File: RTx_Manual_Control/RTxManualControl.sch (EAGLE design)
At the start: 36 parts

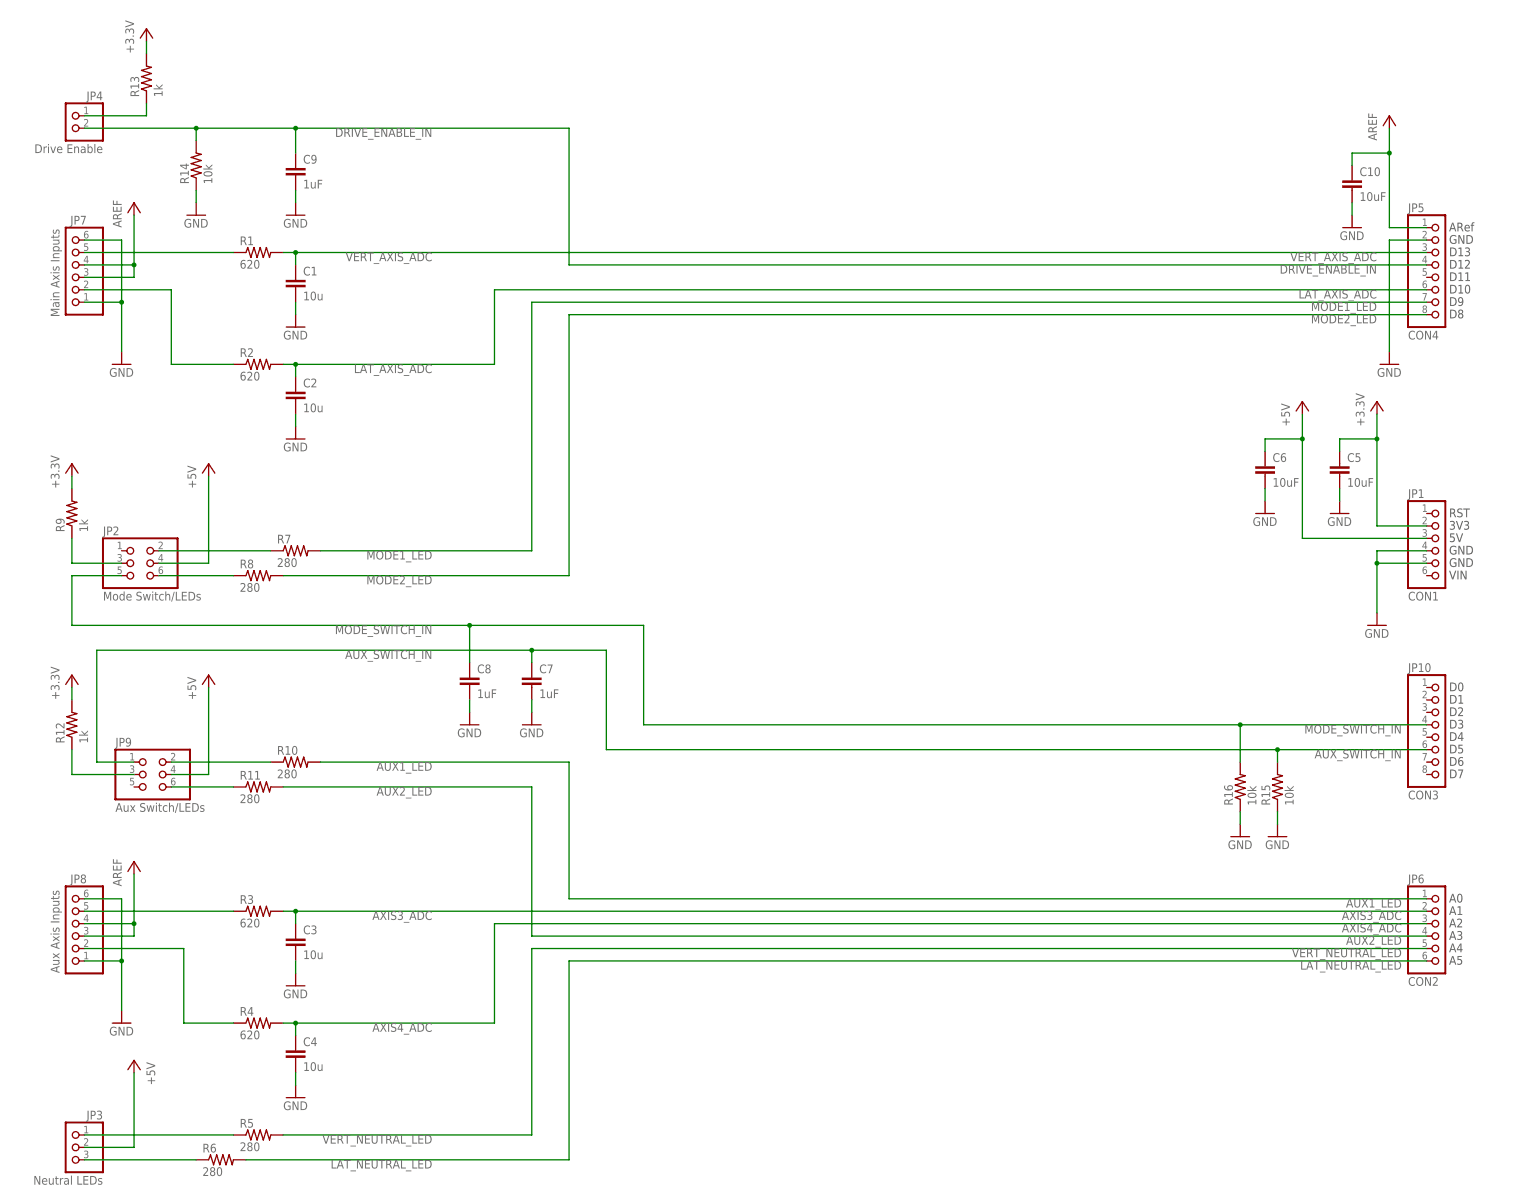
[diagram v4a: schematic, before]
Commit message: Generated BOM for Manual Control board. Corrected capacitor value formatting.
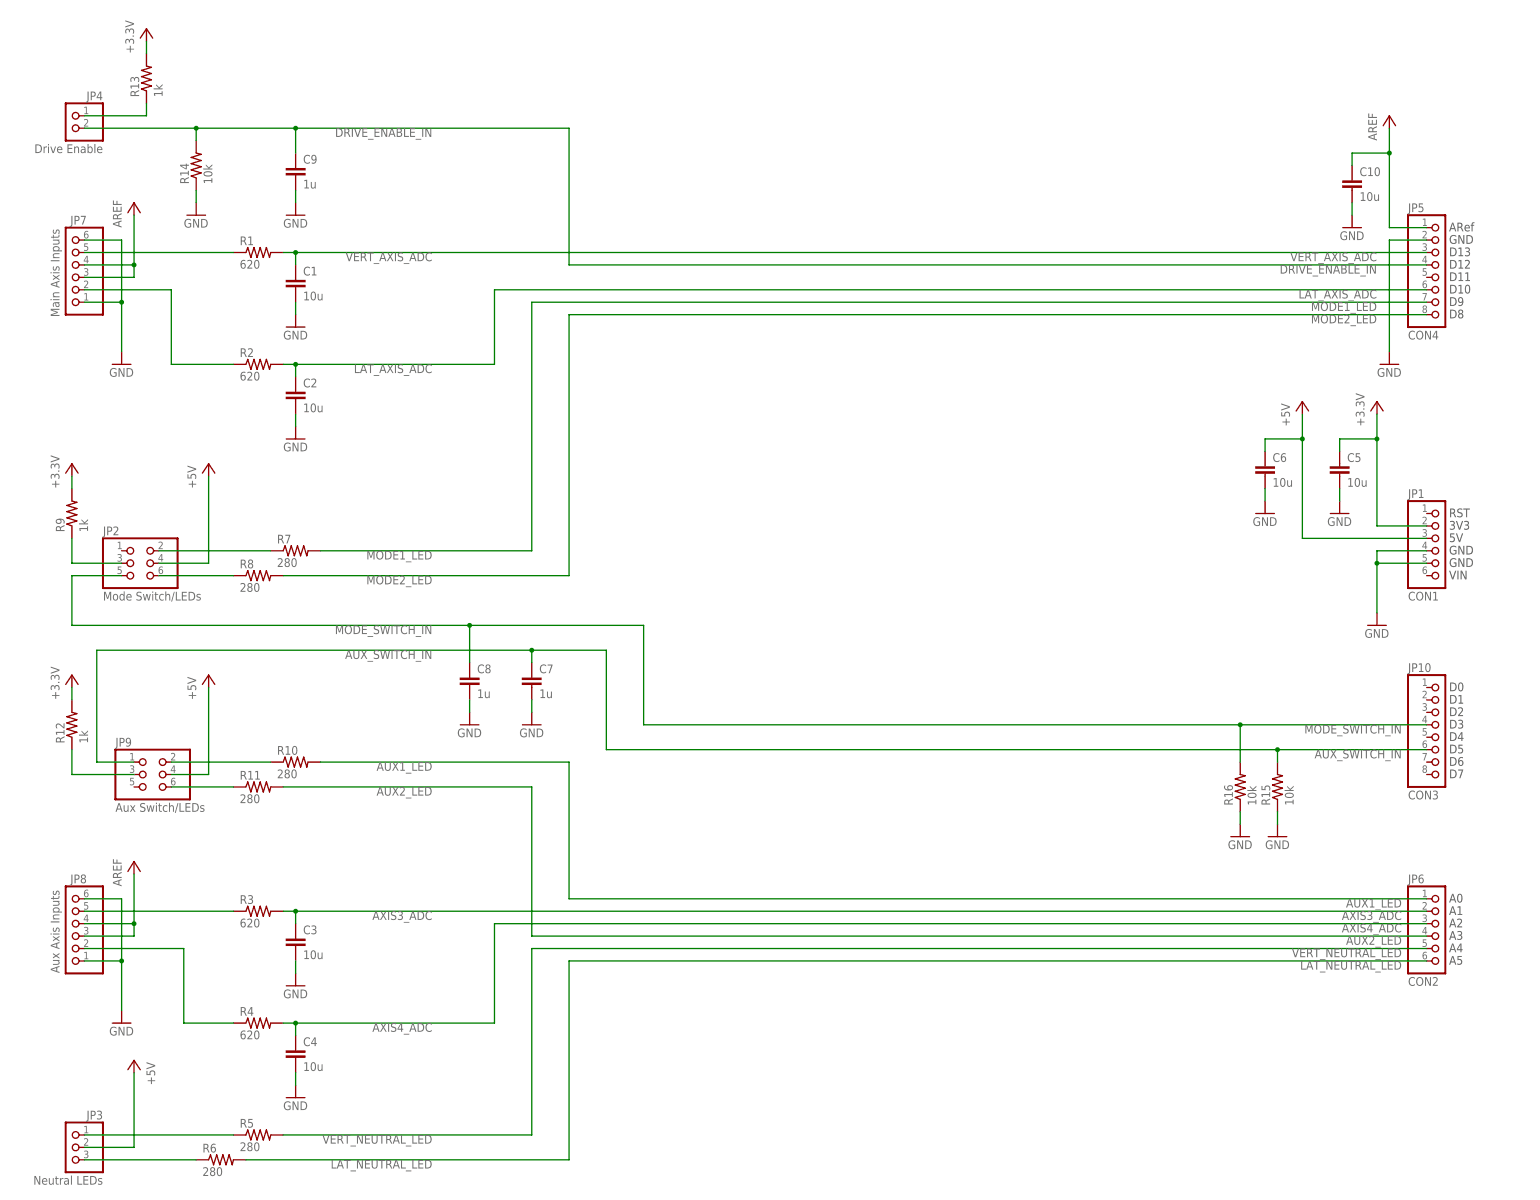
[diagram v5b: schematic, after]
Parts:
- C10, C5, C6: value 10uF -> 10u
- C7, C8, C9: value 1uF -> 1u
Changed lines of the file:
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@@
 <part name="R14" library="rcl" deviceset="R-US_" device="R1206" value="10k"/>
 <part name="GND11" library="supply1" deviceset="GND" device=""/>
-<part name="C5" library="rcl" deviceset="C-EU" device="C1206" value="10uF"/>
+<part name="C5" library="rcl" deviceset="C-EU" device="C1206" value="10u"/>
 <part name="GND12" library="supply1" deviceset="GND" device=""/>
-<part name="C6" library="rcl" deviceset="C-EU" device="C1206" value="10uF"/>
+<part name="C6" library="rcl" deviceset="C-EU" device="C1206" value="10u"/>
 <part name="GND13" library="supply1" deviceset="GND" device=""/>
 <part name="JP10" library="pinhead" deviceset="PINHD-1X8" device="" value="CON3"/>
@@
 <part name="GND9" library="supply1" deviceset="GND" device=""/>
 <part name="GND10" library="supply1" deviceset="GND" device=""/>
-<part name="C7" library="rcl" deviceset="C-EU" device="C1206" value="1uF"/>
-<part name="C8" library="rcl" deviceset="C-EU" device="C1206" value="1uF"/>
+<part name="C7" library="rcl" deviceset="C-EU" device="C1206" value="1u"/>
+<part name="C8" library="rcl" deviceset="C-EU" device="C1206" value="1u"/>
 <part name="GND14" library="supply1" deviceset="GND" device=""/>
 <part name="GND15" library="supply1" deviceset="GND" device=""/>
-<part name="C9" library="rcl" deviceset="C-EU" device="C1206" value="1uF"/>
+<part name="C9" library="rcl" deviceset="C-EU" device="C1206" value="1u"/>
 <part name="GND16" library="supply1" deviceset="GND" device=""/>
-<part name="C10" library="rcl" deviceset="C-EU" device="C1206" value="10uF"/>
+<part name="C10" library="rcl" deviceset="C-EU" device="C1206" value="10u"/>
 <part name="GND17" library="supply1" deviceset="GND" device=""/>
 </parts>
